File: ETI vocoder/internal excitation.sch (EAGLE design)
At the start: 49 parts, among them IC1 LM1458N, IC3 TL081P, IC4 UA741P, IC5 4006N, IC6 4030N, IC7 LM1458N, X1 22-23-2041

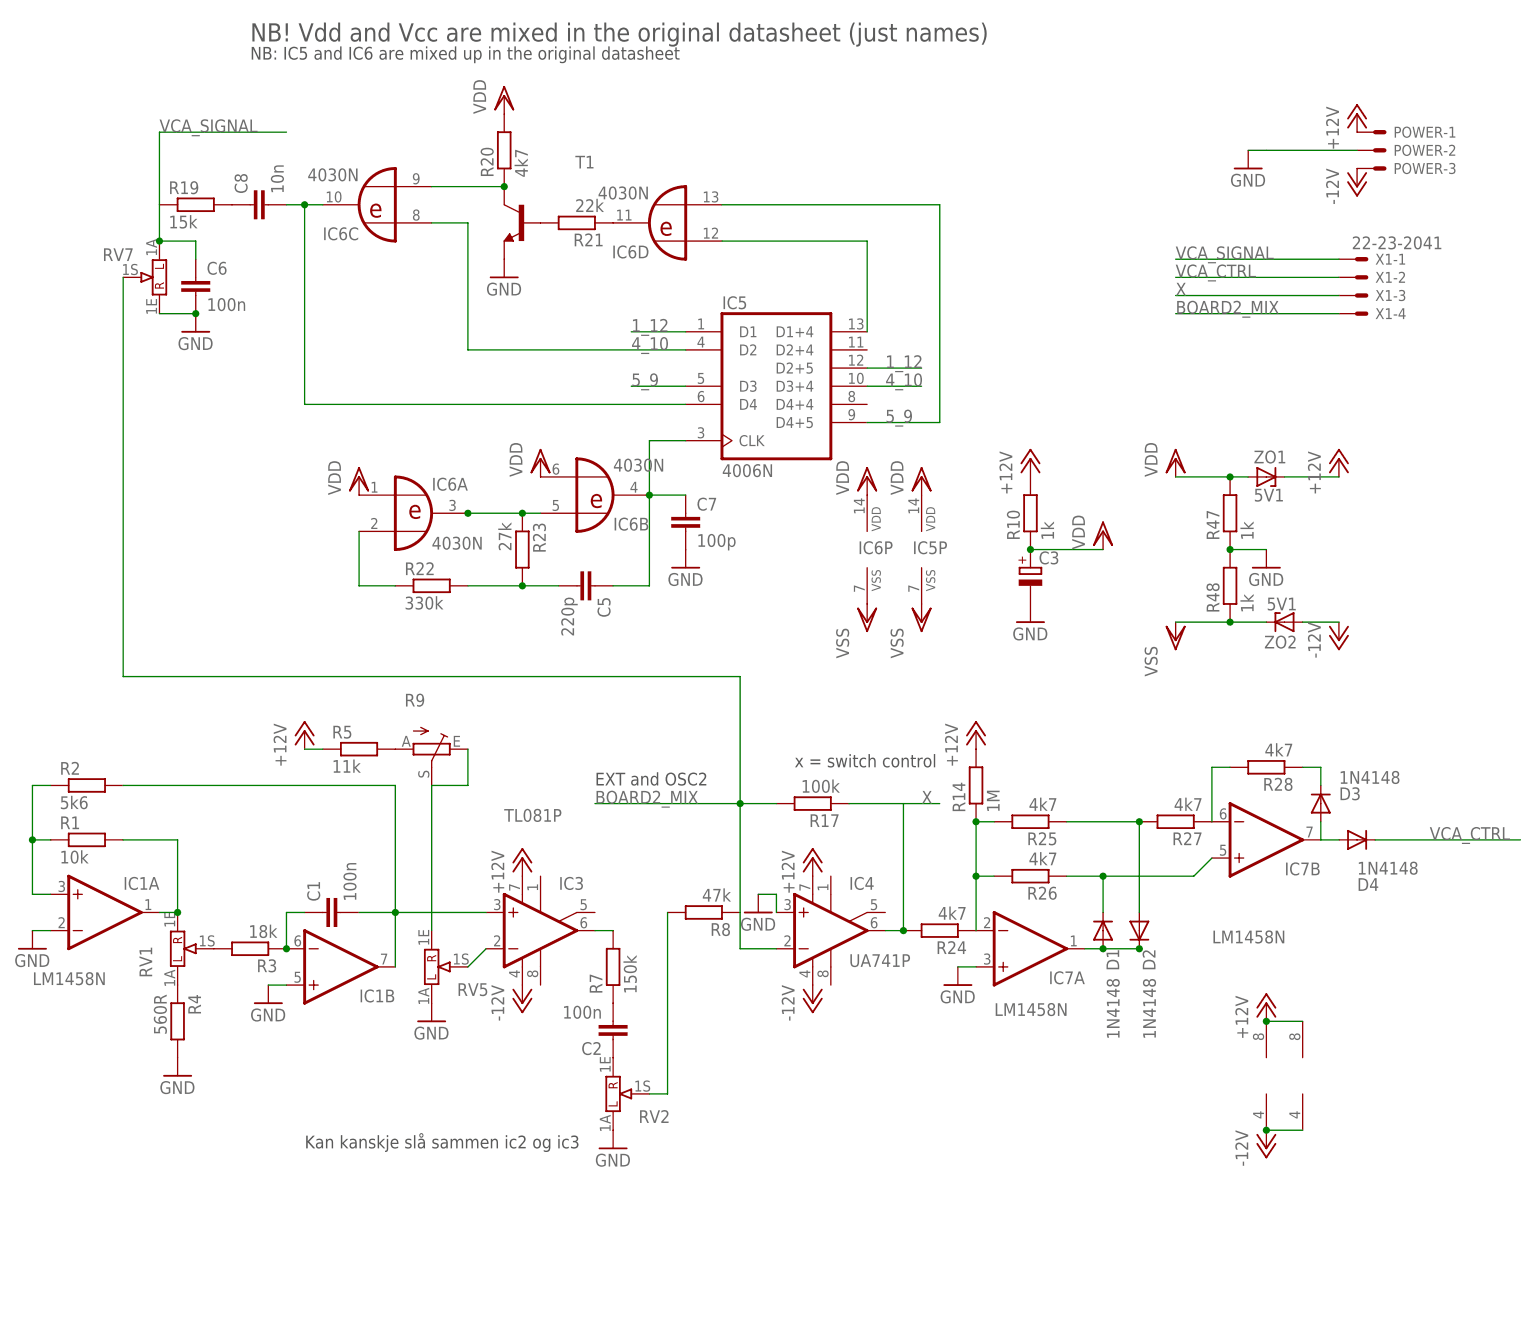
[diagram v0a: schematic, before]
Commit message: Internal excitation schematics
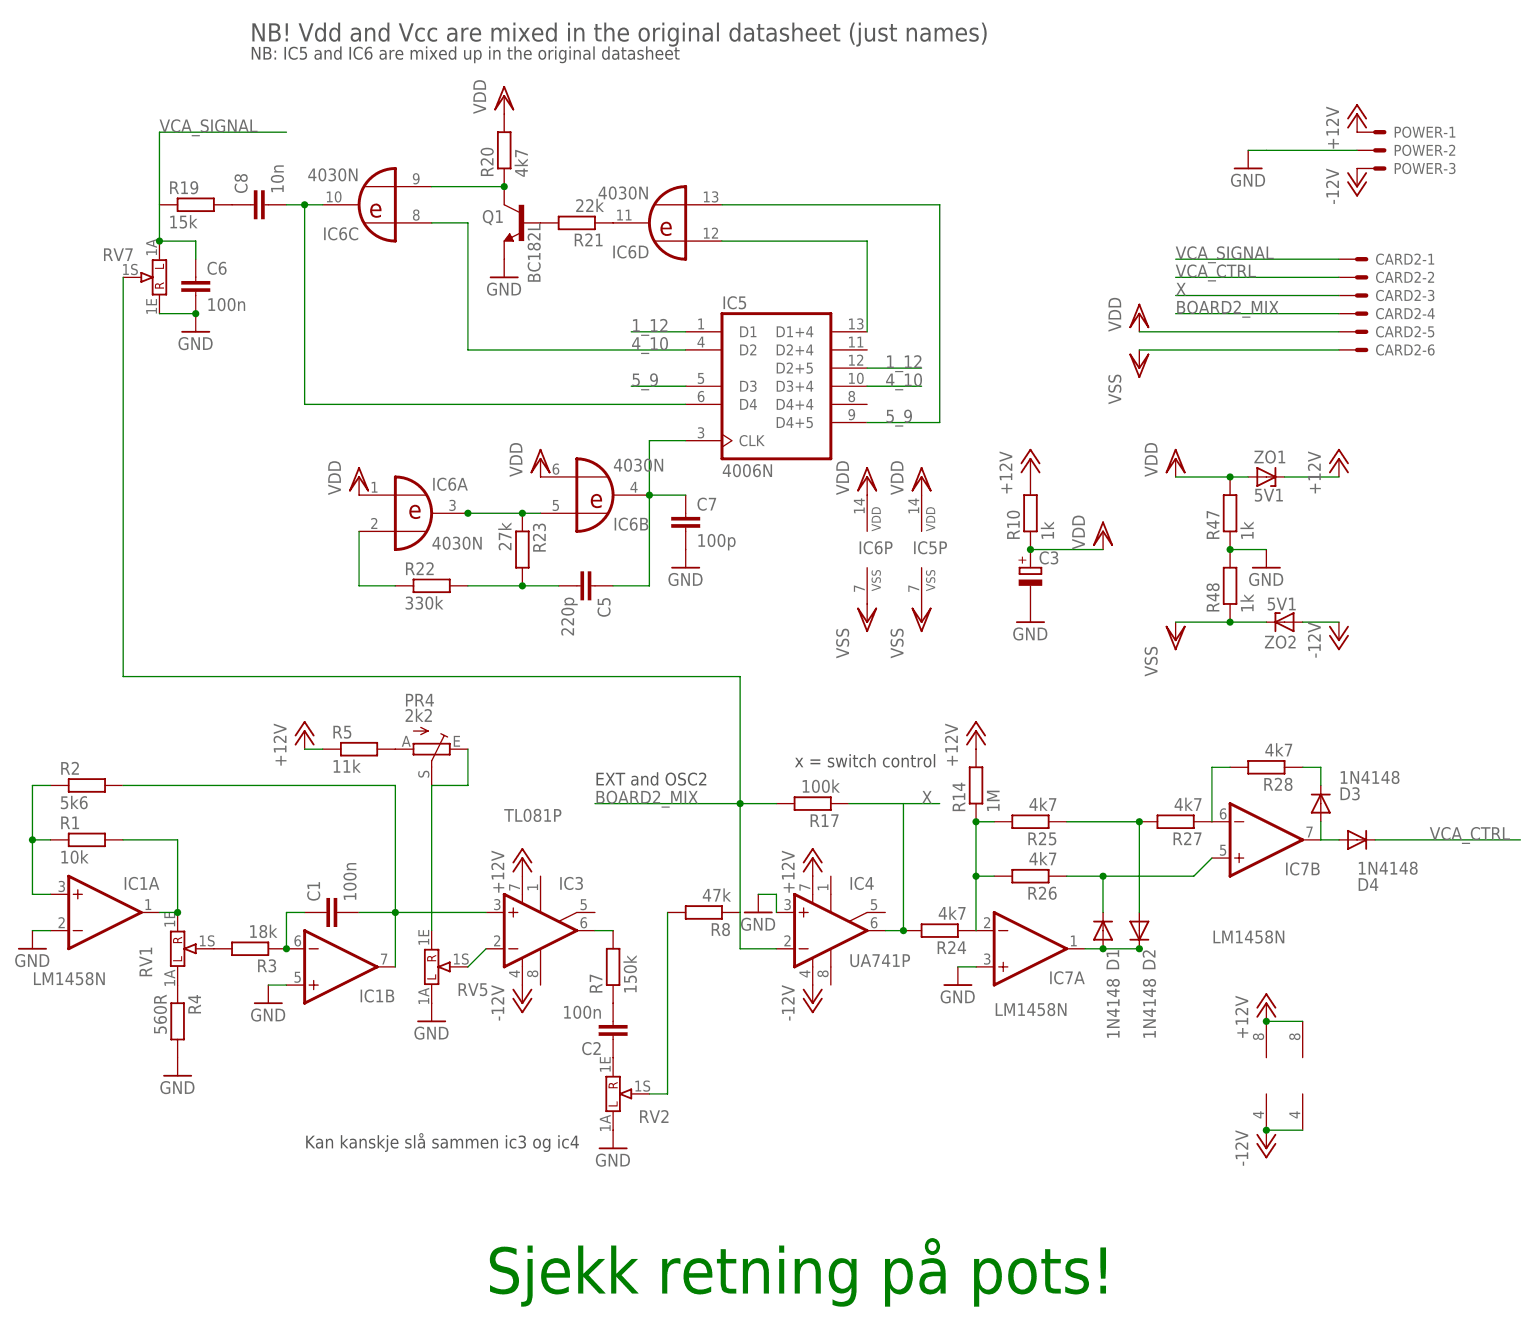
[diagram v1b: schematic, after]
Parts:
- removed X1: 22-23-2041, con-molex:22-23-2041
- added CARD2: (no value), con-molex:22-23-2061
- PR4: value (none) -> 2k2
- Q1: value (none) -> BC182L
- RV2: value 10k -> 10k log
- renumbered R9 to PR4, T1 to Q1
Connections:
- net BOARD2_MIX: now also CARD2-4.S; no longer X1-4.S
- net VCA_CTRL: now also CARD2-2.S; no longer X1-2.S
- net VCA_SIGNAL: now also CARD2-1.S; no longer X1-1.S
- net VDD: now also CARD2-5.S
- net VSS: now also CARD2-6.S
- net X: now also CARD2-3.S; no longer X1-3.S
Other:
- note added: "Kan kanskje slå sammen ic3 og ic4"
- note added: "Sjekk retning på pots!"
- note removed: "Kan kanskje slå sammen ic2 og ic3"
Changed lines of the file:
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@@
 <part name="C1" library="resistor" deviceset="C-EU" device="050-025X075" value="100n"/>
 <part name="RV5" library="joakim" deviceset="POT16_W_BRACKET" device="&quot;&quot;" value="10k"/>
-<part name="R9" library="pot" deviceset="TRIM_EU-" device="CA9V"/>
+<part name="PR4" library="pot" deviceset="TRIM_EU-" device="CA9V" value="2k2"/>
 <part name="P+1" library="supply1" deviceset="+12V" device=""/>
 <part name="P+2" library="supply1" deviceset="+12V" device=""/>
@@
 <part name="GND4" library="supply1" deviceset="GND" device=""/>
 <part name="C2" library="resistor" deviceset="C-EU" device="025-025X050" value="100n"/>
-<part name="RV2" library="joakim" deviceset="POT16_W_BRACKET" device="&quot;&quot;" value="10k"/>
+<part name="RV2" library="joakim" deviceset="POT16_W_BRACKET" device="&quot;&quot;" value="10k log"/>
 <part name="GND5" library="supply1" deviceset="GND" device=""/>
 <part name="GND6" library="supply1" deviceset="GND" device=""/>
@@
 <part name="VDD7" library="supply1" deviceset="VDD" device=""/>
 <part name="C3" library="resistor" deviceset="CPOL-EU" device="E2.5-5"/>
-<part name="T1" library="transistor" deviceset="*-NPN-" device="TO92-ECB"/>
+<part name="Q1" library="transistor" deviceset="*-NPN-" device="TO92-ECB" value="BC182L"/>
 <part name="GND12" library="supply1" deviceset="GND" device=""/>
-<part name="X1" library="con-molex" deviceset="22-23-2041" device=""/>
 <part name="GND13" library="supply1" deviceset="GND" device=""/>
 <part name="POWER" library="con-molex" deviceset="KK-156-3" device=""/>
 <part name="P+8" library="supply1" deviceset="+12V" device=""/>
 <part name="P-5" library="supply1" deviceset="-12V" device=""/>
+<part name="CARD2" library="con-molex" deviceset="22-23-2061" device=""/>
+<part name="VDD8" library="supply1" deviceset="VDD" device=""/>
+<part name="VSS4" library="supply1" deviceset="VSS" device=""/>
 </parts>
 <sheets>
 <sheet>
 <plain>
-<text x="40.64" y="0" size="1.778" layer="97">Kan kanskje slå sammen ic2 og ic3</text>
+<text x="40.64" y="0" size="1.778" layer="97">Kan kanskje slå sammen ic3 og ic4</text>
 <text x="33.02" y="152.4" size="1.778" layer="97">NB: IC5 and IC6 are mixed up in the original datasheet</text>
 <text x="33.02" y="154.94" size="2.54" layer="97">NB! Vdd and Vcc are mixed in the original datasheet (just names)</text>
 <text x="109.22" y="53.34" size="1.778" layer="97">x = switch control</text>
 <text x="81.28" y="50.8" size="1.778" layer="97">EXT and OSC2</text>
+<text x="66.04" y="-20.32" size="6.4516" layer="91">Sjekk retning på pots!</text>
 </plain>
 <instances>
@@
 <attribute name="NAME" x="61.976" y="21.336" size="1.778" layer="95"/>
 </instance>
-<instance part="R9" gate="1" x="58.42" y="55.88" rot="R270"/>
+<instance part="PR4" gate="1" x="58.42" y="55.88" rot="R270"/>
 <instance part="P+1" gate="1" x="40.64" y="58.42"/>
 <instance part="P+2" gate="1" x="71.12" y="40.64"/>
@@
 <instance part="VDD7" gate="G$1" x="152.4" y="86.36"/>
 <instance part="C3" gate="G$1" x="142.24" y="81.28"/>
-<instance part="T1" gate="G$1" x="71.12" y="129.54" rot="MR0"/>
+<instance part="Q1" gate="G$1" x="71.12" y="129.54" smashed="yes" rot="MR0">
+<attribute name="NAME" x="68.58" y="129.54" size="1.778" layer="95" rot="MR0"/>
+<attribute name="VALUE" x="73.66" y="129.54" size="1.778" layer="96" rot="MR270"/>
+</instance>
 <instance part="GND12" gate="1" x="68.58" y="121.92"/>
-<instance part="X1" gate="-1" x="187.96" y="124.46"/>
-<instance part="X1" gate="-2" x="187.96" y="121.92"/>
-<instance part="X1" gate="-3" x="187.96" y="119.38"/>
-<instance part="X1" gate="-4" x="187.96" y="116.84"/>
 <instance part="GND13" gate="1" x="172.72" y="137.16"/>
 <instance part="POWER" gate="-1" x="190.5" y="142.24"/>
@@
 <instance part="P+8" gate="1" x="187.96" y="144.78"/>
 <instance part="P-5" gate="1" x="187.96" y="134.62"/>
+<instance part="CARD2" gate="-1" x="187.96" y="124.46"/>
+<instance part="CARD2" gate="-2" x="187.96" y="121.92"/>
+<instance part="CARD2" gate="-3" x="187.96" y="119.38"/>
+<instance part="CARD2" gate="-4" x="187.96" y="116.84"/>
+<instance part="CARD2" gate="-5" x="187.96" y="114.3"/>
+<instance part="CARD2" gate="-6" x="187.96" y="111.76"/>
+<instance part="VDD8" gate="G$1" x="157.48" y="116.84"/>
+<instance part="VSS4" gate="G$1" x="157.48" y="109.22"/>
 </instances>
 <busses>
@@
 </segment>
 <segment>
-<pinref part="T1" gate="G$1" pin="E"/>
+<pinref part="Q1" gate="G$1" pin="E"/>
 <pinref part="GND12" gate="1" pin="GND"/>
 </segment>
@@
 <net name="N$8" class="0">
 <segment>
-<pinref part="R9" gate="1" pin="A"/>
+<pinref part="PR4" gate="1" pin="A"/>
 <pinref part="R5" gate="G$1" pin="2"/>
 </segment>
@@
 <segment>
 <pinref part="RV5" gate="G$1" pin="1E"/>
-<pinref part="R9" gate="1" pin="S"/>
+<pinref part="PR4" gate="1" pin="S"/>
 <wire x1="58.42" y1="30.48" x2="58.42" y2="50.8" width="0.1524" layer="91"/>
 <wire x1="58.42" y1="50.8" x2="63.5" y2="50.8" width="0.1524" layer="91"/>
-<pinref part="R9" gate="1" pin="E"/>
+<pinref part="PR4" gate="1" pin="E"/>
 <wire x1="63.5" y1="50.8" x2="63.5" y2="55.88" width="0.1524" layer="91"/>
 </segment>
@@
 </segment>
 <segment>
-<pinref part="X1" gate="-4" pin="S"/>
 <wire x1="185.42" y1="116.84" x2="162.56" y2="116.84" width="0.1524" layer="91"/>
 <label x="162.56" y="116.84" size="1.778" layer="95"/>
+<pinref part="CARD2" gate="-4" pin="S"/>
 </segment>
 </net>
@@
 <wire x1="185.42" y1="119.38" x2="162.56" y2="119.38" width="0.1524" layer="91"/>
 <label x="162.56" y="119.38" size="1.778" layer="95"/>
-<pinref part="X1" gate="-3" pin="S"/>
+<pinref part="CARD2" gate="-3" pin="S"/>
 </segment>
 </net>
@@
 <wire x1="185.42" y1="121.92" x2="162.56" y2="121.92" width="0.1524" layer="91"/>
 <label x="162.56" y="121.92" size="1.778" layer="95"/>
-<pinref part="X1" gate="-2" pin="S"/>
+<pinref part="CARD2" gate="-2" pin="S"/>
 </segment>
 </net>
@@
 <wire x1="185.42" y1="124.46" x2="162.56" y2="124.46" width="0.1524" layer="91"/>
 <label x="162.56" y="124.46" size="1.778" layer="95"/>
-<pinref part="X1" gate="-1" pin="S"/>
+<pinref part="CARD2" gate="-1" pin="S"/>
 </segment>
 </net>
@@
 <pinref part="R20" gate="G$1" pin="1"/>
 <wire x1="68.58" y1="134.62" x2="58.42" y2="134.62" width="0.1524" layer="91"/>
-<pinref part="T1" gate="G$1" pin="C"/>
+<pinref part="Q1" gate="G$1" pin="C"/>
 <junction x="68.58" y="134.62"/>
 </segment>
@@
 <junction x="142.24" y="83.82"/>
 </segment>
+<segment>
+<pinref part="CARD2" gate="-5" pin="S"/>
+<wire x1="185.42" y1="114.3" x2="157.48" y2="114.3" width="0.1524" layer="91"/>
+<pinref part="VDD8" gate="G$1" pin="VDD"/>
+</segment>
 </net>
 <net name="VSS" class="0">
@@
 <junction x="170.18" y="73.66"/>
 </segment>
+<segment>
+<pinref part="CARD2" gate="-6" pin="S"/>
+<wire x1="185.42" y1="111.76" x2="157.48" y2="111.76" width="0.1524" layer="91"/>
+<pinref part="VSS4" gate="G$1" pin="VSS"/>
+</segment>
 </net>
 <net name="N$33" class="0">
 <segment>
 <pinref part="R21" gate="G$1" pin="2"/>
-<pinref part="T1" gate="G$1" pin="B"/>
-</segment>
-</net>
+<pinref part="Q1" gate="G$1" pin="B"/>
+</segment>
+</net>
